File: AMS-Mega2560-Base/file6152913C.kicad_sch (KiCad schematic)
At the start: 13 parts, among them IC16 DS3231SN#, IC17 MAX232CPE+, IC19 MAX6326UR31+T, Q24 BS250, U3 S8411-45R

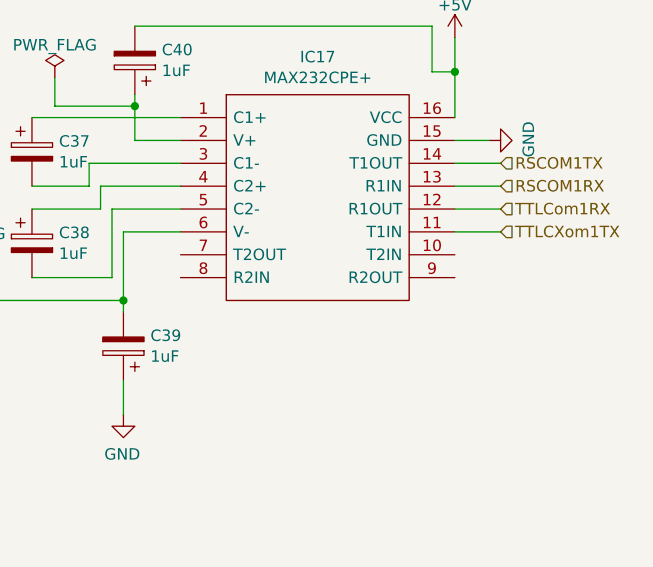
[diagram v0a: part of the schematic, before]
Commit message: wip for adding second rs232 port. needs to have the other end added to an output pin/port
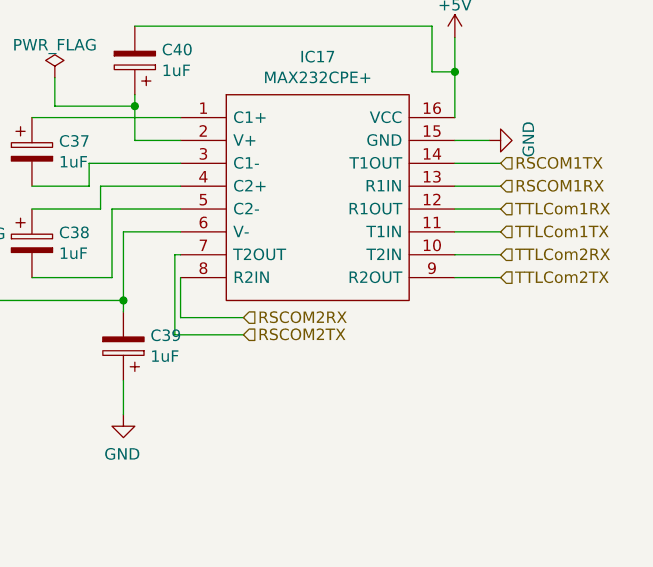
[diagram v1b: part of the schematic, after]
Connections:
- net TTLCom2RX: now reaches IC17.10 (T2IN)
- net RSCOM2TX: now reaches IC17.7 (T2OUT)
- net RSCOM2RX: now reaches IC17.8 (R2IN)
- net TTLCom2TX: now reaches IC17.9 (R2OUT)
- net TTLCXom1TX renamed TTLCom1TX
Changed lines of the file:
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@@
+    (stroke (width 0) (type default) (color 0 0 0 0))
+  )
+  (wire (pts (xy 262.255 50.8) (xy 267.335 50.8))
     (stroke (width 0) (type default) (color 0 0 0 0))
   )
@@
     (stroke (width 0) (type default) (color 0 0 0 0))
   )
+  (wire (pts (xy 262.255 48.26) (xy 267.335 48.26))
+    (stroke (width 0) (type default) (color 0 0 0 0))
+  )
   (wire (pts (xy 215.265 50.8) (xy 224.155 50.8))
     (stroke (width 0) (type default) (color 0 0 0 0))
@@
     (stroke (width 0) (type default) (color 0 0 0 0))
   )
+  (wire (pts (xy 231.14 57.15) (xy 238.76 57.15))
+    (stroke (width 0) (type default) (color 0 0 0 0))
+  )
   (wire (pts (xy 78.74 43.18) (xy 76.2 43.18))
     (stroke (width 0) (type default) (color 0 0 0 0))
@@
     (stroke (width 0) (type default) (color 0 0 0 0))
   )
+  (wire (pts (xy 231.775 55.245) (xy 231.775 50.8))
+    (stroke (width 0) (type default) (color 0 0 0 0))
+  )
   (wire (pts (xy 68.58 58.42) (xy 68.58 55.88))
     (stroke (width 0) (type default) (color 0 0 0 0))
@@
     (stroke (width 0) (type default) (color 0 0 0 0))
   )
+  (wire (pts (xy 238.76 55.245) (xy 231.775 55.245))
+    (stroke (width 0) (type default) (color 0 0 0 0))
+  )
   (wire (pts (xy 69.85 24.13) (xy 69.85 20.32))
     (stroke (width 0) (type default) (color 0 0 0 0))
   )
+  (wire (pts (xy 231.14 48.26) (xy 231.14 57.15))
+    (stroke (width 0) (type default) (color 0 0 0 0))
+  )
+  (wire (pts (xy 231.775 48.26) (xy 231.14 48.26))
+    (stroke (width 0) (type default) (color 0 0 0 0))
+  )
   (wire (pts (xy 133.985 67.31) (xy 133.985 99.695))
     (stroke (width 0) (type default) (color 0 0 0 0))
   )
+  (hierarchical_label "RSCOM2TX" (shape input) (at 238.76 57.15 0)
+    (effects (font (size 1.27 1.27)) (justify left))
+  )
   (hierarchical_label "TTLCom1RX" (shape input) (at 267.335 43.18 0)
     (effects (font (size 1.27 1.27)) (justify left))
@@
     (effects (font (size 1.27 1.27)) (justify left))
   )
-  (hierarchical_label "TTLCXom1TX" (shape input) (at 267.335 45.72 0)
+  (hierarchical_label "TTLCom1TX" (shape input) (at 267.335 45.72 0)
+    (effects (font (size 1.27 1.27)) (justify left))
+  )
+  (hierarchical_label "TTLCom2TX" (shape input) (at 267.335 50.8 0)
     (effects (font (size 1.27 1.27)) (justify left))
   )
@@
     (effects (font (size 1.27 1.27)) (justify left))
   )
+  (hierarchical_label "TTLCom2RX" (shape input) (at 267.335 48.26 0)
+    (effects (font (size 1.27 1.27)) (justify left))
+  )
   (hierarchical_label "RSCOM1TX" (shape input) (at 267.335 38.1 0)
     (effects (font (size 1.27 1.27)) (justify left))
   )
+  (hierarchical_label "RSCOM2RX" (shape input) (at 238.76 55.245 0)
+    (effects (font (size 1.27 1.27)) (justify left))
+  )

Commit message: working on this.
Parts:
- removed C36: 0.1uF, Capacitor_THT:C_Rect_L9.0mm_W3.6mm_P7.50mm_MKT, symbol Device:C
- removed D10: 1N4001, Diode_THT:D_DO-41_SOD81_P10.16mm_Horizontal, symbol Diode:1N4001
- removed IC16: DS3231SN#, SamacSys_Parts:SOIC127P1032X265-16N, symbol SamacSys_Parts:DS3231SN#
- removed IC19: MAX6326UR31+T, SOT95P237X112-3N, symbol Samac_Sys:MAX6326UR31+T
- removed Q24: BS250, Package_TO_SOT_THT:TO-92_Inline, symbol Transistor_FET:BS250
- removed R37, R38: 10k, Resistor_THT:R_Axial_DIN0207_L6.3mm_D2.5mm_P2.54mm_Vertical, symbol Device:R
- removed U3: S8411-45R, SamacSys_Parts:S8411-45R_1, symbol SamacSys_Parts:S8411-45R
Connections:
- no-connect marks 3 -> 0
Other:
- moved on the sheet: C37, C38, C39, C40, IC17
